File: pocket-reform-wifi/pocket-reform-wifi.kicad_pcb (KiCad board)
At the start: 4 copper layers, 27.6 x 95 mm, 42 parts, among them J1 Bus_M.2_Socket_E, J2 Conn_01x20, J21 CONN_HEAD, J22 SJ-43516-SMT, J24 CONN_PWRSW, SW21 SW_DIP_x01, U1 TPS62A04ABDRL, X1 ECS-327MVATX-2-CN-TR3

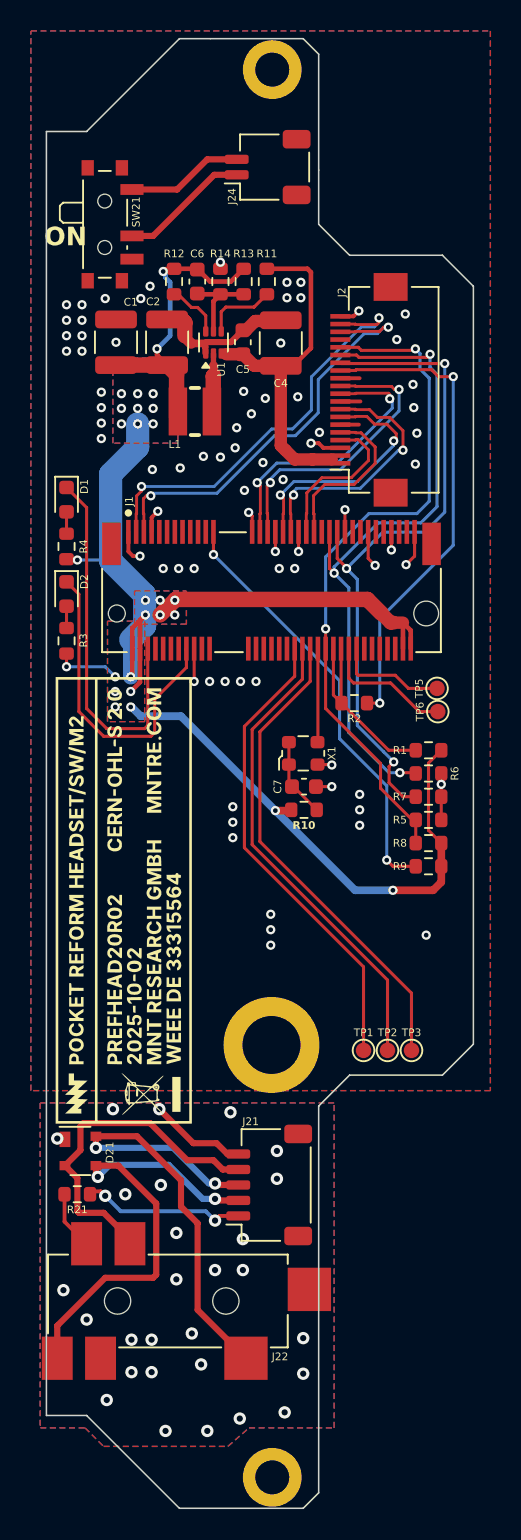
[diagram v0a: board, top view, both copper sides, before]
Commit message: wifi/headset board: move screw holes by -0.5mm for better fit (r3)
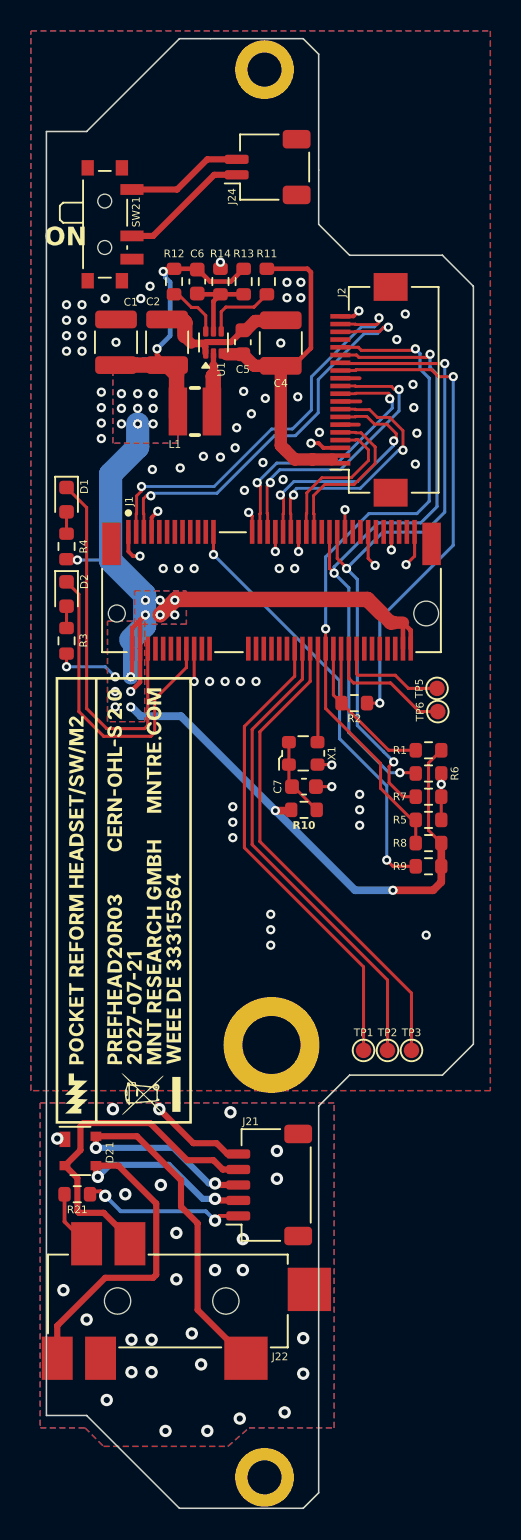
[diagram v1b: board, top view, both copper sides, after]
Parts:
- GFX21: footprint footprints:pref-headset-badge -> footprints:pref-headset-badge-r3
- moved H21 0.50 mm to (99.5, 79.0)
- moved H22 0.50 mm to (99.5, 170.0)
